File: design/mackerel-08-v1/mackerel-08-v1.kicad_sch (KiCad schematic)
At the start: 17 parts, among them U1 MC68008, U2 7410, U3 74HC595, U4 SST39SF040, U5 AS7C4096A, U6 XR68C681, U7 GAL16V8, X1 CXO_DIP14, X2 CXO_DIP8

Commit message: Added most of the PLDs to the schematic
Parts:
- removed R5: R, Resistor_THT:R_Axial_DIN0207_L6.3mm_D2.5mm_P7.62mm_Horizontal, symbol Device:R
- removed U2: 7410, Package_DIP:DIP-14_W7.62mm, symbol 74xx_IEEE:7410
- added U? (x6): AS7C4096A, symbol mackerel-68k-symbols:AS7C4096A
- added U? (x2): GAL16V8, Package_DIP:DIP-20_W7.62mm, symbol Logic_Programmable:GAL16V8
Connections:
- net +5V: now also U4.31 (PGM), U5.27 (VCC), U5.9 (VCC), U?.20 (VCC), U?.20 (VCC), U?.27 (VCC), U?.27 (VCC), U?.27 (VCC), U?.27 (VCC), U?.27 (VCC), U?.27 (VCC), U?.9 (VCC), U?.9 (VCC), U?.9 (VCC), U?.9 (VCC), U?.9 (VCC), U?.9 (VCC)
- net GND: now also U4.24 (OE), U5.10 (GND), U5.28 (GND), U5.31 (OE), U7.1 (I1/CLK), U7.11 (I10/~{OE}), U7.6 (I6), U?.1 (I1/CLK), U?.10 (GND), U?.10 (GND), U?.10 (GND), U?.10 (GND), U?.10 (GND), U?.10 (GND), U?.10 (GND), U?.10 (GND), U?.11 (I10/~{OE}), U?.28 (GND), U?.28 (GND), U?.28 (GND), U?.28 (GND), U?.28 (GND), U?.28 (GND), U?.31 (OE), U?.31 (OE), U?.31 (OE), U?.31 (OE), U?.31 (OE), U?.31 (OE), U?.6 (I6), U?.7 (I7), U?.8 (I8), U?.9 (I9)
- net /IACK: now also U7.19 (IO1), U?.3 (I3)
- net /IPL0: now also U?.14 (IO6)
- net /IPL1: now also U?.15 (IO5)
- net /IPL2: now also U?.16 (IO4)
- net /IACK7: now reaches U7.12 (IO8)
- net /IACK6: now reaches U7.13 (IO7)
- net /IACK5: now reaches U7.14 (IO6)
- net /IACK4: now reaches U7.15 (IO5)
- net /IACK3: now reaches U7.16 (IO4)
- net /IACK2: now reaches U7.17 (I03)
- net /IACK1: now reaches U7.18 (IO2)
- net /IACK1: now also U6.41 (/IACK)
- net /AS: now reaches U7.2 (I2)
- net /AS: now also U1.31 (/AS), U?.2 (I2)
- net A1: now reaches U7.3 (I3)
- net A1: now also U1.52 (A1), U4.11 (A1), U5.2 (A1), U6.2 (A1), U?.2 (A1), U?.2 (A1), U?.2 (A1), U?.2 (A1), U?.2 (A1), U?.2 (A1)
- net A2: now reaches U7.4 (I4)
- net A2: now also U1.1 (A2), U4.10 (A2), U5.3 (A2), U6.4 (A2), U?.3 (A2), U?.3 (A2), U?.3 (A2), U?.3 (A2), U?.3 (A2), U?.3 (A2)
- net A3: now reaches U7.5 (I5)
- net A3: now also U1.2 (A3), U4.9 (A3), U5.4 (A3), U6.6 (A3), U?.4 (A3), U?.4 (A3), U?.4 (A3), U?.4 (A3), U?.4 (A3), U?.4 (A3)
- net FC0: now reaches U7.7 (I7)
- net FC0: now also U1.50 (FC0)
- net FC1: now reaches U7.8 (I8)
- net FC1: now also U1.49 (FC1)
- net FC2: now reaches U7.9 (I9)
- net FC2: now also U1.48 (FC2)
- net D1: now reaches U6.18 (D1)
- net D1: now also U1.29 (D1), U4.14 (D1), U5.8 (IO2), U?.8 (IO2), U?.8 (IO2), U?.8 (IO2), U?.8 (IO2), U?.8 (IO2), U?.8 (IO2)
- net D3: now reaches U6.19 (D3)
- net D3: now also U1.27 (D3), U4.17 (D3), U5.12 (IO4), U?.12 (IO4), U?.12 (IO4), U?.12 (IO4), U?.12 (IO4), U?.12 (IO4), U?.12 (IO4)
- net D5: now reaches U6.20 (D5)
- net D5: now also U1.25 (D5), U4.19 (D5), U5.26 (IO6), U?.26 (IO6), U?.26 (IO6), U?.26 (IO6), U?.26 (IO6), U?.26 (IO6), U?.26 (IO6)
- net D7: now reaches U6.21 (D7)
- net D7: now also U1.23 (D7), U4.21 (D7), U5.30 (IO8), U?.30 (IO8), U?.30 (IO8), U?.30 (IO8), U?.30 (IO8), U?.30 (IO8), U?.30 (IO8)
- net /IRQ1: now reaches U6.24 (INTR)
- net /IRQ1: now also U?.4 (I4)
- net D6: now reaches U6.25 (D6)
- net D6: now also U1.24 (D6), U4.20 (D6), U5.29 (IO7), U?.29 (IO7), U?.29 (IO7), U?.29 (IO7), U?.29 (IO7), U?.29 (IO7), U?.29 (IO7)
- net D4: now reaches U6.26 (D4)
- net D4: now also U1.26 (D4), U4.18 (D4), U5.25 (IO5), U?.25 (IO5), U?.25 (IO5), U?.25 (IO5), U?.25 (IO5), U?.25 (IO5), U?.25 (IO5)
- net D2: now reaches U6.27 (D2)
- net D2: now also U1.28 (D2), U4.15 (D2), U5.11 (IO3), U?.11 (IO3), U?.11 (IO3), U?.11 (IO3), U?.11 (IO3), U?.11 (IO3), U?.11 (IO3)
- net D0: now reaches U6.28 (D0)
- net D0: now also U1.30 (D0), U4.13 (D0), U5.7 (IO1), U?.7 (IO1), U?.7 (IO1), U?.7 (IO1), U?.7 (IO1), U?.7 (IO1), U?.7 (IO1)
- net A4: now reaches U6.7 (A4)
- net A4: now also U1.3 (A4), U4.8 (A4), U5.5 (A4), U?.5 (A4), U?.5 (A4), U?.5 (A4), U?.5 (A4), U?.5 (A4), U?.5 (A4)
- net /RW: now reaches U6.9 (/RW)
- net /RW: now also U1.33 (/RW), U5.13 (WE), U?.13 (WE), U?.13 (WE), U?.13 (WE), U?.13 (WE), U?.13 (WE), U?.13 (WE)
- net A18: now reaches U4.1 (A18)
- net A18: now also U1.20 (A18), U5.35 (A18), U?.35 (A18), U?.35 (A18), U?.35 (A18), U?.35 (A18), U?.35 (A18), U?.35 (A18), U?.9 (I9)
- net A0: now reaches U4.12 (A0)
- net A0: now also U1.51 (A0), U5.1 (A0), U?.1 (A0), U?.1 (A0), U?.1 (A0), U?.1 (A0), U?.1 (A0), U?.1 (A0)
- net A16: now reaches U4.2 (A16)
- net A16: now also U1.18 (A16), U5.33 (A16), U?.33 (A16), U?.33 (A16), U?.33 (A16), U?.33 (A16), U?.33 (A16), U?.33 (A16), U?.7 (I7)
- net ROM_EN: now reaches U4.22 (CE)
- net ROM_EN: now also U?.17 (I03)
- net A10: now reaches U4.23 (A10)
- net A10: now also U1.9 (A10), U5.20 (A10), U?.20 (A10), U?.20 (A10), U?.20 (A10), U?.20 (A10), U?.20 (A10), U?.20 (A10)
- net A11: now reaches U4.25 (A11)
- net A11: now also U1.10 (A11), U5.21 (A11), U?.21 (A11), U?.21 (A11), U?.21 (A11), U?.21 (A11), U?.21 (A11), U?.21 (A11)
- net A9: now reaches U4.26 (A9)
- net A9: now also U1.8 (A9), U5.18 (A9), U?.18 (A9), U?.18 (A9), U?.18 (A9), U?.18 (A9), U?.18 (A9), U?.18 (A9)
- net A8: now reaches U4.27 (A8)
- net A8: now also U1.7 (A8), U5.17 (A8), U?.17 (A8), U?.17 (A8), U?.17 (A8), U?.17 (A8), U?.17 (A8), U?.17 (A8)
- net A13: now reaches U4.28 (A13)
- net A13: now also U1.12 (A13), U5.23 (A13), U?.23 (A13), U?.23 (A13), U?.23 (A13), U?.23 (A13), U?.23 (A13), U?.23 (A13)
- net A14: now reaches U4.29 (A14)
- net A14: now also U1.14 (A14), U5.24 (A14), U?.24 (A14), U?.24 (A14), U?.24 (A14), U?.24 (A14), U?.24 (A14), U?.24 (A14)
- net A15: now reaches U4.3 (A15)
- net A15: now also U1.16 (A15), U5.32 (A15), U?.32 (A15), U?.32 (A15), U?.32 (A15), U?.32 (A15), U?.32 (A15), U?.32 (A15)
- net A17: now reaches U4.30 (A17)
- net A17: now also U1.19 (A17), U5.34 (A17), U?.34 (A17), U?.34 (A17), U?.34 (A17), U?.34 (A17), U?.34 (A17), U?.34 (A17), U?.8 (I8)
- net A12: now reaches U4.4 (A12)
- net A12: now also U1.11 (A12), U5.22 (A12), U?.22 (A12), U?.22 (A12), U?.22 (A12), U?.22 (A12), U?.22 (A12), U?.22 (A12)
- net A7: now reaches U4.5 (A7)
- net A7: now also U1.6 (A7), U5.16 (A7), U?.16 (A7), U?.16 (A7), U?.16 (A7), U?.16 (A7), U?.16 (A7), U?.16 (A7)
- net A6: now reaches U4.6 (A6)
- net A6: now also U1.5 (A6), U5.15 (A6), U?.15 (A6), U?.15 (A6), U?.15 (A6), U?.15 (A6), U?.15 (A6), U?.15 (A6)
- net A5: now reaches U4.7 (A5)
- net A5: now also U1.4 (A5), U5.14 (A5), U?.14 (A5), U?.14 (A5), U?.14 (A5), U?.14 (A5), U?.14 (A5), U?.14 (A5)
- net A21: now reaches U1.13 (A21)
- net A21: now also U?.13 (IO7), U?.5 (I5)
- net A19: now reaches U1.21 (A19)
- net A19: now also U?.11 (I10/~{OE}), U?.3 (I3)
- net A20: now reaches U1.22 (A20)
- net A20: now also U?.12 (IO8), U?.4 (I4)
- net RAM_EN0: now reaches U5.6 (CE)
- net RAM_EN0: now also U?.19 (IO1)
- new net BOOT: U?.1 (I1/CLK)
- new net IO_EN: U?.19 (IO1)
- new net RAM_EN: U?.18 (IO2), U?.2 (I2)
- new net RAM_EN1: U?.18 (IO2), U?.6 (CE)
- new net RAM_EN2: U?.17 (I03), U?.6 (CE)
- new net RAM_EN3: U?.16 (IO4), U?.6 (CE)
- new net RAM_EN4: U?.15 (IO5), U?.6 (CE)
- new net RAM_EN5: U?.14 (IO6), U?.6 (CE)
- new net RAM_EN6: U?.13 (IO7), U?.6 (CE)
- new net /IRQ2: U?.5 (I5)
- new net /IRQ3: U?.6 (I6)
- no-connect marks 7 -> 6
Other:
- note added: "Address/Interrupt Decoder"
- note added: "IACK Decoder"
- note added: "RAM Chip Selector"
- note added: "TODO: Double check the RAM/ROM/IO enable lines"
- note added: "TODO: decode IO_EN into multiple peripherals"
- note added: "TODO: might make sense to move IACK back to NAND gate"
- note added: "TODO: probe pins"
- moved on the sheet: R1, R2, R3, R4, R6, R7, R8, U1, U3, U4, U5, U6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

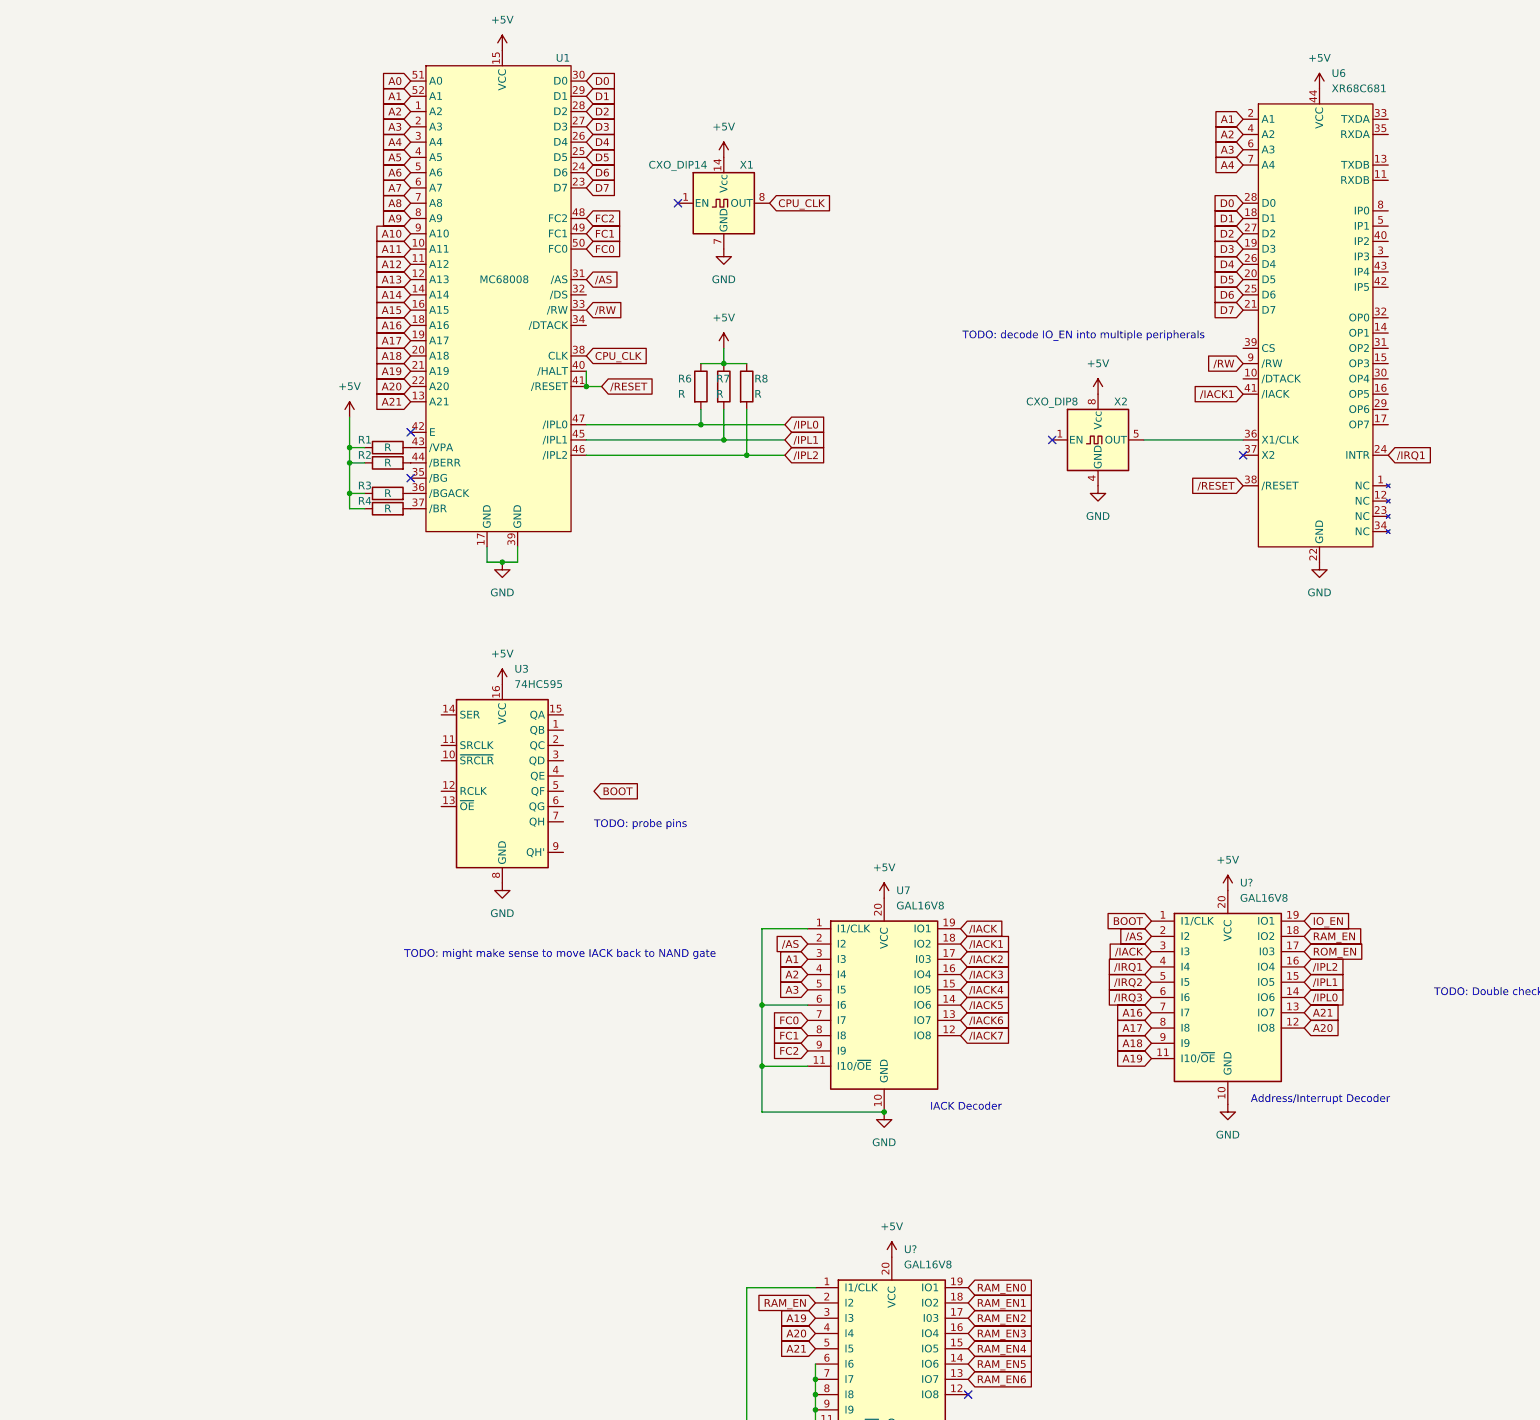
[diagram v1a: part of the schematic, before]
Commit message: Cleaned up the rest of the PLD logic equations and schematic
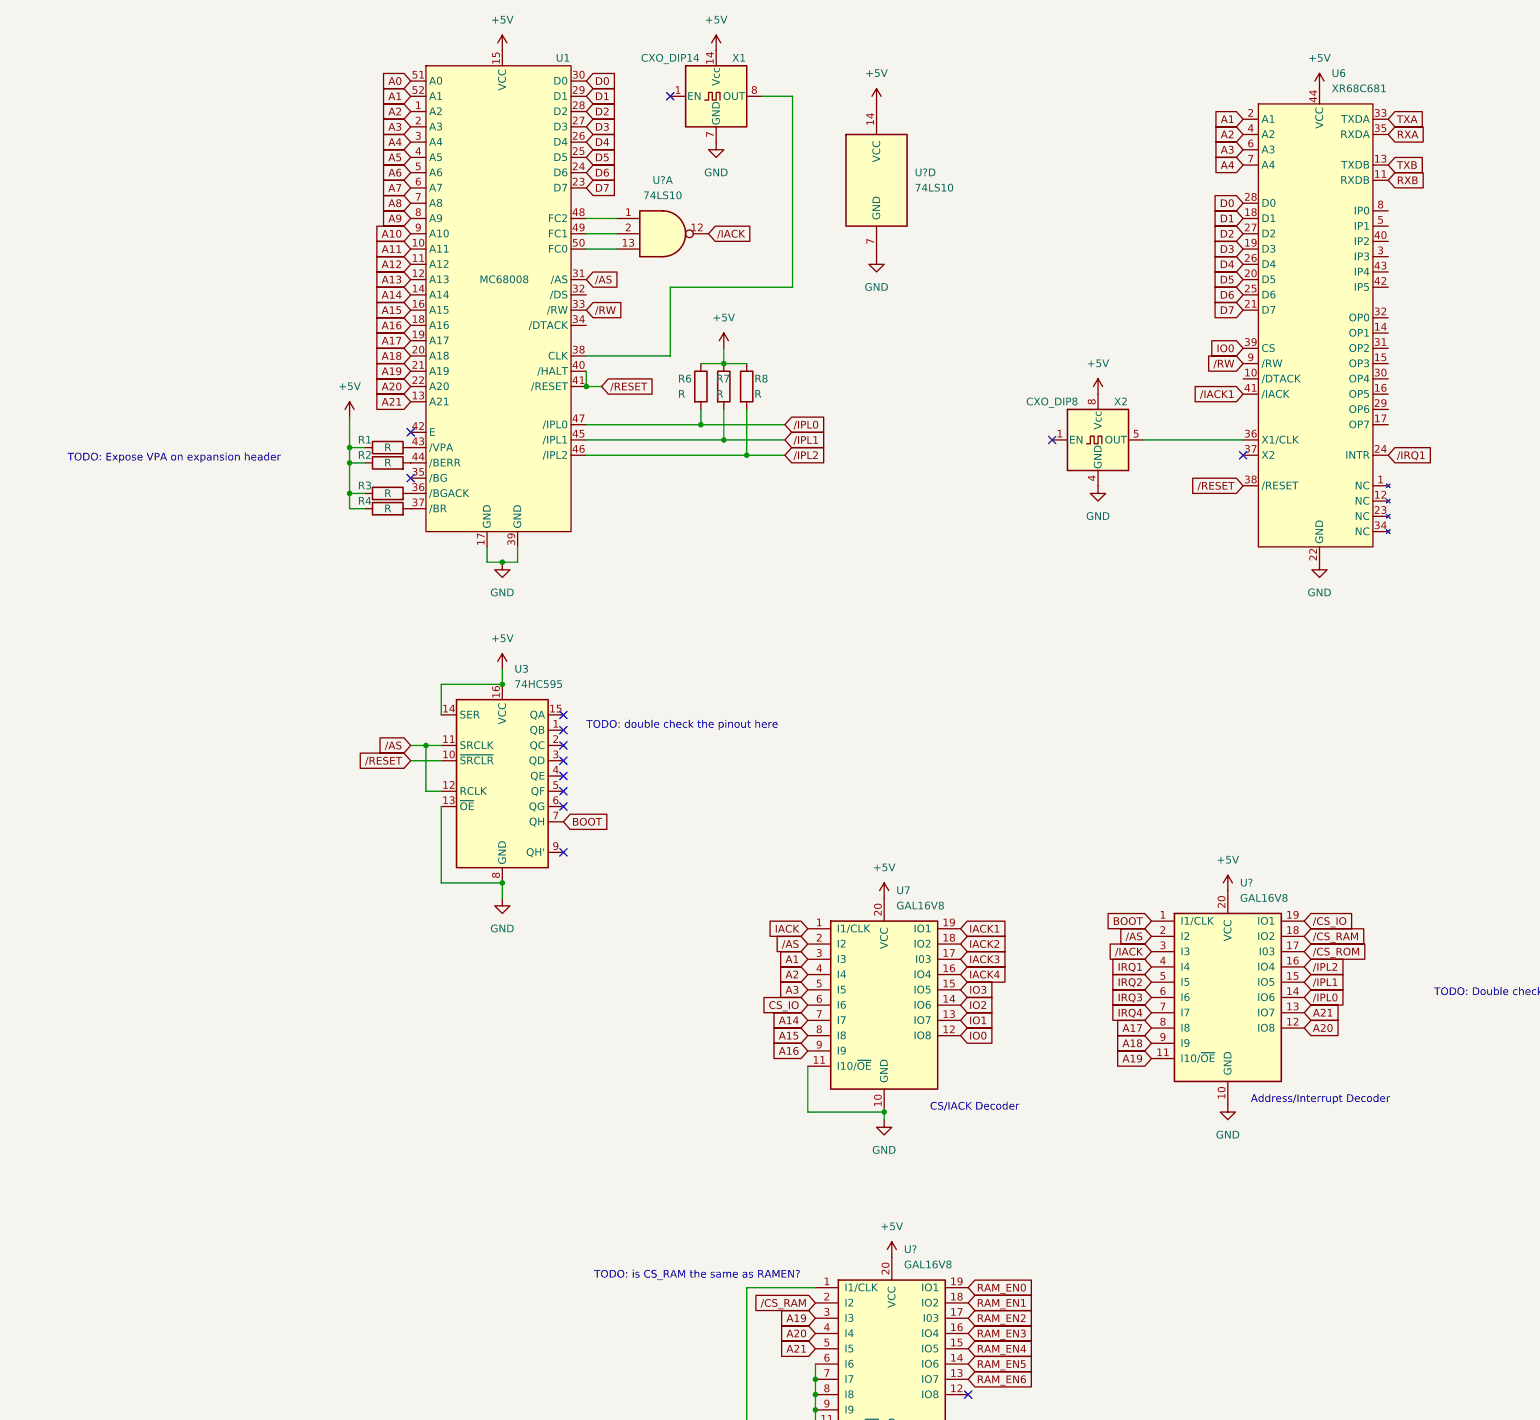
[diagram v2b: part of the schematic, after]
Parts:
- added U? (x2): 74LS10, symbol 74xx:74LS10
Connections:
- net /IACK7 is gone; now on net IO0: U7.12 (IO8)
- net +5V: now also U3.14 (SER), U?.14 (VCC)
- net A14: now also U7.7 (I7)
- net A15: now also U7.8 (I8)
- net A16: now also U7.9 (I9); no longer U?.7 (I7)
- net BOOT: now also U3.7 (QH)
- net GND: now also U3.13 (~{OE}), U?.7 (GND); no longer U7.1 (I1/CLK), U7.6 (I6)
- net ROM_EN: no longer U?.17 (I03)
- net /AS: now also U3.11 (SRCLK), U3.12 (RCLK)
- net /IACK: now also U?.12; no longer U7.19 (IO1)
- net /IACK1: no longer U7.18 (IO2)
- net /IRQ1: no longer U?.4 (I4)
- net /RESET: now also U3.10 (~{SRCLR})
- net RXB: now reaches U6.11 (RXDB)
- net TXB: now reaches U6.13 (TXDB)
- net TXA: now reaches U6.33 (TXDA)
- net RXA: now reaches U6.35 (RXDA)
- net IO0: now reaches U6.39 (CS)
- net CPU_CLK: no longer names the net of U1.38 (CLK), X1.8 (OUT)
- net FC0: no longer names the net of U1.50 (FC0)
- net FC0: now also U?.13; no longer U7.7 (I7)
- net FC1: no longer names the net of U1.49 (FC1)
- net FC1: now also U?.2; no longer U7.8 (I8)
- net FC2: no longer names the net of U1.48 (FC2)
- net FC2: now also U?.1; no longer U7.9 (I9)
- net IO_EN renamed /CS_IO
- net RAM_EN renamed /CS_RAM
- net /IACK2 renamed IACK3
- net /IACK3 renamed IACK4
- net /IACK4 renamed IO3
- net /IACK5 renamed IO2
- net /IACK6 renamed IO1
- net /IRQ2 renamed IRQ2
- net /IRQ3 renamed IRQ3
- new net CS_IO: U7.6 (I6)
- new net IACK: U7.1 (I1/CLK)
- new net IACK1: U7.19 (IO1)
- new net IACK2: U7.18 (IO2)
- new net IRQ1: U?.4 (I4)
- new net IRQ4: U?.7 (I7)
- new net /CS_ROM: U?.17 (I03)
- no-connect marks 6 -> 14
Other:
- note added: "CS/IACK Decoder"
- note added: "TODO: Expose VPA on expansion header"
- note added: "TODO: double check the pinout here"
- note added: "TODO: is CS_RAM the same as RAMEN?"
- note removed: "IACK Decoder"
- note removed: "TODO: decode IO_EN into multiple peripherals"
- note removed: "TODO: might make sense to move IACK back to NAND gate"
- note removed: "TODO: probe pins"
- moved on the sheet: X1

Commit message: simplifying schematic
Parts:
- removed R3, R4: R, Resistor_THT:R_Axial_DIN0207_L6.3mm_D2.5mm_P7.62mm_Horizontal, symbol Device:R
- removed U4: SST39SF040, Socket:DIP_Socket-32_W11.9_W12.7_W15.24_W17.78_W18.5_3M_232-1285-00-0602J, symbol Memory_Flash:SST39SF040
- removed U7: GAL16V8, Package_DIP:DIP-20_W7.62mm, symbol Logic_Programmable:GAL16V8
- removed U? (x2): 74LS10, symbol 74xx:74LS10
- removed U?: AS7C4096A, symbol mackerel-68k-symbols:AS7C4096A
- removed X1: CXO_DIP14, Oscillator:Oscillator_DIP-14, symbol Oscillator:CXO_DIP14
- added C1: C_Polarized, Capacitor_THT:CP_Radial_D5.0mm_P2.50mm, symbol Device:C_Polarized
- added C2: C_Polarized, Capacitor_THT:CP_Radial_D8.0mm_P3.80mm, symbol Device:C_Polarized
- added D1, D2: LED, LED_THT:LED_D5.0mm, symbol Device:LED
- added J2: DC_Jack, Connector_BarrelJack:BarrelJack_GCT_DCJ200-10-A_Horizontal, symbol mackerel-68k-symbols:DC_Jack
- added J3, J4: Conn_01x06, Connector_PinHeader_2.54mm:PinHeader_1x06_P2.54mm_Vertical, symbol Connector_Generic:Conn_01x06
- added J5: Conn_02x20_Odd_Even, Connector_PinHeader_2.54mm:PinHeader_2x20_P2.54mm_Vertical, symbol Connector_Generic:Conn_02x20_Odd_Even
- added R10, R11, R12, R13, R6, R7, R8, R9: R, Resistor_SMD:R_1206_3216Metric_Pad1.30x1.75mm_HandSolder, symbol Device:R
- added SW1: SW_Push, Button_Switch_THT:SW_PUSH_6mm_H5mm, symbol Switch:SW_Push
- added U11: 74HC10, Package_DIP:DIP-14_W7.62mm_Socket_LongPads, symbol mackerel-68k-symbols:74HC10
- added U14: NE555P, Package_DIP:DIP-8_W7.62mm, symbol Timer:NE555P
- added U8: SST39SF040, Package_DIP:DIP-32_W15.24mm_Socket_LongPads, symbol mackerel-68k-symbols:SST39SF040
- added X1: CXO_DIP8, Oscillator:Oscillator_DIP-8, symbol Oscillator:CXO_DIP8
- R1, R2: footprint Resistor_THT:R_Axial_DIN0207_L6.3mm_D2.5mm_P7.62mm_Horizontal -> Resistor_SMD:R_1206_3216Metric_Pad1.30x1.75mm_HandSolder
- R3: renamed from R6; footprint Resistor_THT:R_Axial_DIN0207_L6.3mm_D2.5mm_P7.62mm_Horizontal -> Resistor_SMD:R_1206_3216Metric_Pad1.30x1.75mm_HandSolder
- R4: renamed from R7; footprint Resistor_THT:R_Axial_DIN0207_L6.3mm_D2.5mm_P7.62mm_Horizontal -> Resistor_SMD:R_1206_3216Metric_Pad1.30x1.75mm_HandSolder
- R5: renamed from R8; footprint Resistor_THT:R_Axial_DIN0207_L6.3mm_D2.5mm_P7.62mm_Horizontal -> Resistor_SMD:R_1206_3216Metric_Pad1.30x1.75mm_HandSolder
- U10: renamed from U3; footprint Package_DIP:DIP-16_W7.62mm -> Package_DIP:DIP-16_W7.62mm_Socket_LongPads
- U12, U13: renamed from U?; footprint Package_DIP:DIP-20_W7.62mm -> Package_DIP:DIP-20_W7.62mm_Socket_LongPads
- U2: renamed from U5; footprint (none) -> Package_SO:SOJ-36_10.16x23.49mm_P1.27mm
- U3, U4, U5, U6, U7: renamed from U?; footprint (none) -> Package_SO:SOJ-36_10.16x23.49mm_P1.27mm
- renumbered U6 to U9
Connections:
- net IRQ2 is gone; now on net A1: U12.5 (I5)
- net IRQ3 is gone; now on net A2: U12.6 (I6)
- net IRQ4 is gone; now on net A3: U12.7 (I7)
- net /IACK1 is gone; now on net /IACK_DUART: U9.41 (/IACK)
- net /IRQ1 is gone; now on net /IRQ_DUART: U9.24 (INTR)
- net +5V: now also R2.2, C1.1, C2.1, J2.1 (VCC), R10.1, R11.1, R13.1, R6.2, R7.2, R8.2, R9.2, U11.14 (VCC), U14.8 (VCC), U8.31 (/WE), U8.32 (VCC), X1.8 (Vcc); no longer R1.1, R2.1
- net A0: now also U8.12 (A0)
- net A1: now also U8.11 (A1)
- net A10: now also U8.23 (A10)
- net A11: now also U8.25 (A11)
- net A12: now also U8.4 (A12)
- net A13: now also U8.28 (A13)
- net A14: now also U8.29 (A14)
- net A15: now also U8.3 (A15)
- net A16: now also U8.2 (A16)
- net A17: now also U8.30 (A17)
- net A18: now also U8.1 (A18)
- net A2: now also U8.10 (A2)
- net A3: now also U8.9 (A3)
- net A4: now also U8.8 (A4)
- net A5: now also U8.7 (A5)
- net A6: now also U8.6 (A6)
- net A7: now also U8.5 (A7)
- net A8: now also U8.27 (A8)
- net A9: now also U8.26 (A9)
- net D0: now also U8.13 (D0)
- net D1: now also U8.14 (D1)
- net D2: now also U8.15 (D2)
- net D3: now also U8.17 (D3)
- net D4: now also U8.18 (D4)
- net D5: now also U8.19 (D5)
- net D6: now also U8.20 (D6)
- net D7: now also U8.21 (D7)
- net GND: now also R1.1, C2.2, D2.1 (K), J2.2 (GND), J3.6 (Pin_6), J4.6 (Pin_6), R12.2, SW1.1, U11.1 (1A), U11.10 (3B), U11.11 (3C), U11.13 (1C), U11.2 (1B), U11.7 (GND), U11.9 (3A), U14.1 (GND), U8.16 (GND), U8.24 (/OE), X1.4 (GND)
- net RXA: now also J3.3 (Pin_3)
- net RXB: now also J4.3 (Pin_3)
- net TXA: now also J3.2 (Pin_2)
- net TXB: now also J4.2 (Pin_2)
- net /AS: now also J5.24 (Pin_24)
- net /CS_RAM: now also U12.17 (I03); no longer U12.18 (IO2)
- net /CS_ROM: now also U12.16 (IO4), U8.22 (/CE); no longer U12.17 (I03)
- net /IACK: now also U11.6 (2Y)
- net /IPL1: no longer U12.15 (IO5)
- net /IPL2: no longer U12.16 (IO4)
- net /RESET: now also D1.1 (K), J5.22 (Pin_22), U14.3 (Q)
- net /RW: now also J5.28 (Pin_28)
- net CLK_DUART: now reaches U9.36 (X1/CLK), X2.5 (OUT)
- net at U1.44 (/BERR): now also R9.1; no longer R2.2
- net at U1.36 (/BGACK): now also R8.1
- net at U1.43 (/VPA): now also R6.1; no longer R1.2
- net /DS: now reaches U1.32 (/DS)
- net /DS: now also J5.26 (Pin_26)
- net /DTACK: now reaches U1.34 (/DTACK)
- net /DTACK: now also R1.2, J5.30 (Pin_30)
- net at U1.37 (/BR): now also R7.1
- net at U1.38 (CLK): now also X1.5 (OUT)
- net FC2: now reaches U1.48 (FC2)
- net FC2: now also U11.5 (2C)
- net FC1: now reaches U1.49 (FC1)
- net FC1: now also U11.4 (2B)
- net FC0: now reaches U1.50 (FC0)
- net FC0: now also U11.3 (2A)
- net IO0 renamed /CS_DUART
- net /CS_DUART: now also U12.18 (IO2)
- net IRQ1 renamed /IRQ_DUART
- net RAM_EN6: no longer names the net of U13.13 (IO7)
- net /CS_IO renamed /IACK_DUART
- net /IACK_DUART: now also R2.1
- new net: D1.2 (A), R10.2
- new net: C1.2, R12.1, U14.2 (TR), U14.6 (THR)
- new net: R13.2, SW1.2, U14.4 (R)
- new net: D2.2 (A), R11.2
- no-connect marks 14 -> 76
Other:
- note added: "TODO: expose GPIO pins"
- note added: "TODO: is AS the correct pin here?"
- note added: "TODO: redo this bus layout"
- note removed: "CS/IACK Decoder"
- note removed: "TODO: Double check the RAM/ROM/IO enable lines"
- note removed: "TODO: Expose VPA on expansion header"
- note removed: "TODO: is CS_RAM the same as RAMEN?"
- moved on the sheet: R3, R4, R5, U1, U10, U12, U13, U6, U7, U9, X2
